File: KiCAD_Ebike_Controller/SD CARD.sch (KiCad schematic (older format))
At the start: 5 parts

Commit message: schem done
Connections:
- net labels removed: +3.3V
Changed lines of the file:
@@
 	3050 3300 3150 3400
-$Comp
-L power:+3.3V #PWR?
-U 1 1 5FAF998F
-P 5250 2750
-F 0 "#PWR?" H 5250 2600 50  0001 C CNN
-F 1 "+3.3V" H 5265 2923 50  0000 C CNN
-F 2 "" H 5250 2750 50  0001 C CNN
-F 3 "" H 5250 2750 50  0001 C CNN
-	1    5250 2750
-	1    0    0    -1
-$EndComp
 $Comp
 L power:GND #PWR?
@@
 Wire Wire Line
 	5400 3400 5100 3400
+Text Label 2950 1350 0    50   ~ 0
++3.3v
 Wire Bus Line
 	3050 3100 3050 3700
-Text Label 2950 1350 0    50   ~ 0
+Text Label 5250 2750 0    50   ~ 0
 +3.3v
 $EndSCHEMATC

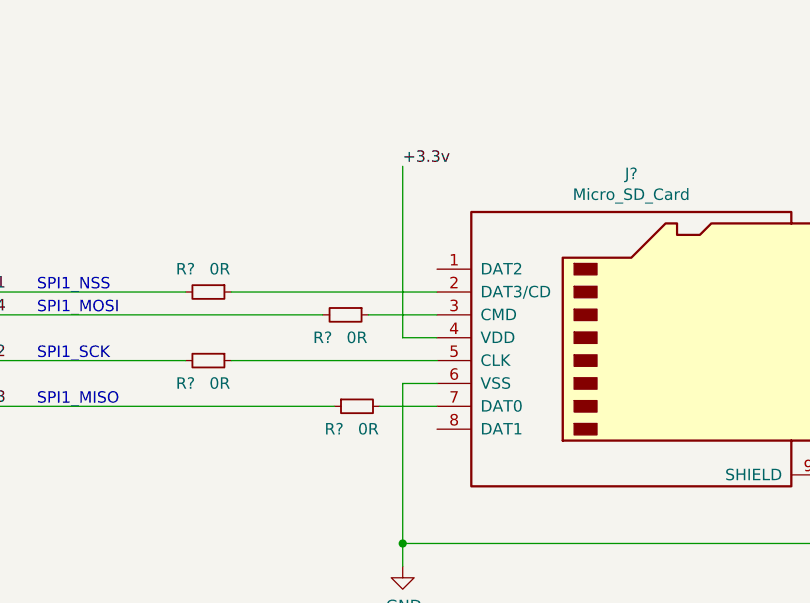
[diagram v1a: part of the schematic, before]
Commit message: adding footprints
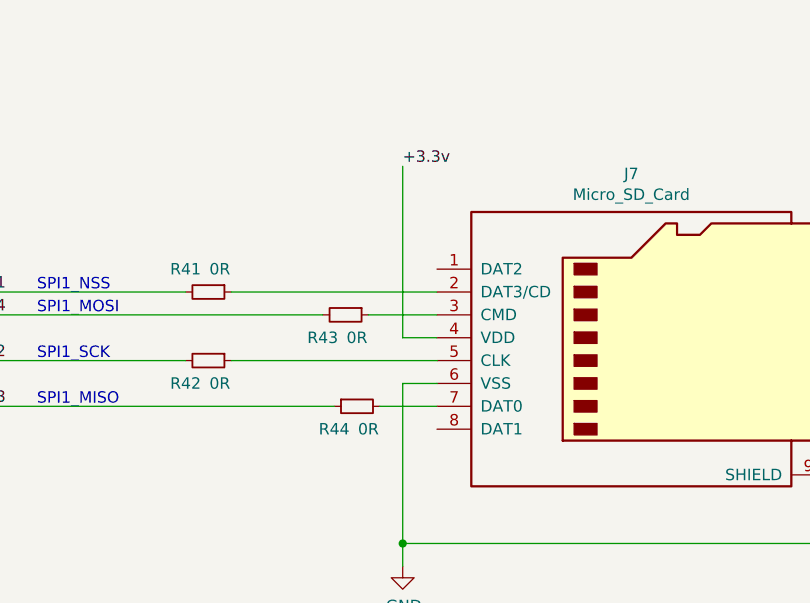
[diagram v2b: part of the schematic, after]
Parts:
- gave numbers to parts that had none: 5
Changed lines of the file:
@@
 	2950 1900 2950 2100
 $Comp
-L power:GND #PWR?
+L power:GND #PWR0129
 U 1 1 5FAEA30A
 P 2950 2100
-F 0 "#PWR?" H 2950 1850 50  0001 C CNN
+F 0 "#PWR0129" H 2950 1850 50  0001 C CNN
 F 1 "GND" H 2955 1927 50  0000 C CNN
 F 2 "" H 2950 2100 50  0001 C CNN
@@
 	3050 3300 3150 3400
 $Comp
-L power:GND #PWR?
+L power:GND #PWR0130
 U 1 1 5FAF9C96
 P 5250 4500
-F 0 "#PWR?" H 5250 4250 50  0001 C CNN
+F 0 "#PWR0130" H 5250 4250 50  0001 C CNN
 F 1 "GND" H 5255 4327 50  0000 C CNN
 F 2 "" H 5250 4500 50  0001 C CNN
@@
 	5250 4400 5250 4500
 $Comp
-L Connector:Micro_SD_Card J?
+L Connector:Micro_SD_Card J7
 U 1 1 5FAFB70A
 P 6300 3500
-F 0 "J?" H 6250 4217 50  0000 C CNN
+F 0 "J7" H 6250 4217 50  0000 C CNN
 F 1 "Micro_SD_Card" H 6250 4126 50  0000 C CNN
 F 2 "" H 7450 3800 50  0001 C CNN
@@
 $EndComp
 $Comp
-L Device:R_Small R?
+L Device:R_Small R41
 U 1 1 5FB009D5
 P 4400 3300
-F 0 "R?" V 4300 3200 50  0000 C CNN
+F 0 "R41" V 4300 3200 50  0000 C CNN
 F 1 "0R" V 4300 3350 50  0000 C CNN
 F 2 "" H 4400 3300 50  0001 C CNN
@@
 $EndComp
 $Comp
-L Device:R_Small R?
+L Device:R_Small R43
 U 1 1 5FB01074
 P 5000 3400
-F 0 "R?" V 5100 3300 50  0000 C CNN
+F 0 "R43" V 5100 3300 50  0000 C CNN
 F 1 "0R" V 5100 3450 50  0000 C CNN
 F 2 "" H 5000 3400 50  0001 C CNN
@@
 $EndComp
 $Comp
-L Device:R_Small R?
+L Device:R_Small R42
 U 1 1 5FB01354
 P 4400 3600
-F 0 "R?" V 4500 3500 50  0000 C CNN
+F 0 "R42" V 4500 3500 50  0000 C CNN
 F 1 "0R" V 4500 3650 50  0000 C CNN
 F 2 "" H 4400 3600 50  0001 C CNN
@@
 $EndComp
 $Comp
-L Device:R_Small R?
+L Device:R_Small R44
 U 1 1 5FB0153E
 P 5050 3800
-F 0 "R?" V 5150 3900 50  0000 C CNN
+F 0 "R44" V 5150 3900 50  0000 C CNN
 F 1 "0R" V 5150 3750 50  0000 C CNN
 F 2 "" H 5050 3800 50  0001 C CNN

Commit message: 50% of the way through the layout
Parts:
- J7: footprint (none) -> Connector_Card:microSD_HC_Hirose_DM3D-SF
- R41, R42, R43, R44: footprint (none) -> Resistor_SMD:R_0805_2012Metric_Pad1.15x1.40mm_HandSolder
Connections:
- net 3.3V+ renamed +3.3V
- net GND renamed GNDD
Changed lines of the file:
@@
 $Descr A4 11693 8268
 encoding utf-8
-Sheet 5 7
+Sheet 6 7
 Title ""
 Date ""
@@
 SPI
 Text HLabel 2500 1500 0    50   Input ~ 0
-3.3V+
++3.3V
 Wire Wire Line
 	2950 1500 2950 1350
@@
 Wire Wire Line
 	2950 1900 2950 2100
-$Comp
-L power:GND #PWR0129
-U 1 1 5FAEA30A
-P 2950 2100
-F 0 "#PWR0129" H 2950 1850 50  0001 C CNN
-F 1 "GND" H 2955 1927 50  0000 C CNN
-F 2 "" H 2950 2100 50  0001 C CNN
-F 3 "" H 2950 2100 50  0001 C CNN
-	1    2950 2100
-	1    0    0    -1
-$EndComp
 Wire Bus Line
 	2400 3100 3050 3100
@@
 Entry Wire Line
 	3050 3300 3150 3400
-$Comp
-L power:GND #PWR0130
-U 1 1 5FAF9C96
-P 5250 4500
-F 0 "#PWR0130" H 5250 4250 50  0001 C CNN
-F 1 "GND" H 5255 4327 50  0000 C CNN
-F 2 "" H 5250 4500 50  0001 C CNN
-F 3 "" H 5250 4500 50  0001 C CNN
-	1    5250 4500
-	1    0    0    -1
-$EndComp
 Wire Wire Line
 	7100 4100 7200 4100
@@
 F 0 "J7" H 6250 4217 50  0000 C CNN
 F 1 "Micro_SD_Card" H 6250 4126 50  0000 C CNN
-F 2 "" H 7450 3800 50  0001 C CNN
+F 2 "Connector_Card:microSD_HC_Hirose_DM3D-SF" H 7450 3800 50  0001 C CNN
 F 3 "http://katalog.we-online.de/em/datasheet/693072010801.pdf" H 6300 3500 50  0001 C CNN
 	1    6300 3500
@@
 F 0 "R41" V 4300 3200 50  0000 C CNN
 F 1 "0R" V 4300 3350 50  0000 C CNN
-F 2 "" H 4400 3300 50  0001 C CNN
+F 2 "Resistor_SMD:R_0805_2012Metric_Pad1.15x1.40mm_HandSolder" H 4400 3300 50  0001 C CNN
 F 3 "~" H 4400 3300 50  0001 C CNN
 	1    4400 3300
@@
 F 0 "R43" V 5100 3300 50  0000 C CNN
 F 1 "0R" V 5100 3450 50  0000 C CNN
-F 2 "" H 5000 3400 50  0001 C CNN
+F 2 "Resistor_SMD:R_0805_2012Metric_Pad1.15x1.40mm_HandSolder" H 5000 3400 50  0001 C CNN
 F 3 "~" H 5000 3400 50  0001 C CNN
 	1    5000 3400
@@
 F 0 "R42" V 4500 3500 50  0000 C CNN
 F 1 "0R" V 4500 3650 50  0000 C CNN
-F 2 "" H 4400 3600 50  0001 C CNN
+F 2 "Resistor_SMD:R_0805_2012Metric_Pad1.15x1.40mm_HandSolder" H 4400 3600 50  0001 C CNN
 F 3 "~" H 4400 3600 50  0001 C CNN
 	1    4400 3600
@@
 F 0 "R44" V 5150 3900 50  0000 C CNN
 F 1 "0R" V 5150 3750 50  0000 C CNN
-F 2 "" H 5050 3800 50  0001 C CNN
+F 2 "Resistor_SMD:R_0805_2012Metric_Pad1.15x1.40mm_HandSolder" H 5050 3800 50  0001 C CNN
 F 3 "~" H 5050 3800 50  0001 C CNN
 	1    5050 3800
@@
 Text Label 2950 1350 0    50   ~ 0
 +3.3v
+Text Label 5250 2750 0    50   ~ 0
++3.3v
 Wire Bus Line
 	3050 3100 3050 3700
-Text Label 5250 2750 0    50   ~ 0
-+3.3v
+$Comp
+L power:GNDD #PWR0130
+U 1 1 5FEADF63
+P 2950 2100
+F 0 "#PWR0130" H 2950 1850 50  0001 C CNN
+F 1 "GNDD" H 2954 1945 50  0000 C CNN
+F 2 "" H 2950 2100 50  0001 C CNN
+F 3 "" H 2950 2100 50  0001 C CNN
+	1    2950 2100
+	1    0    0    -1
+$EndComp
+Text HLabel 5250 4500 0    50   Input ~ 0
+GND
 $EndSCHEMATC

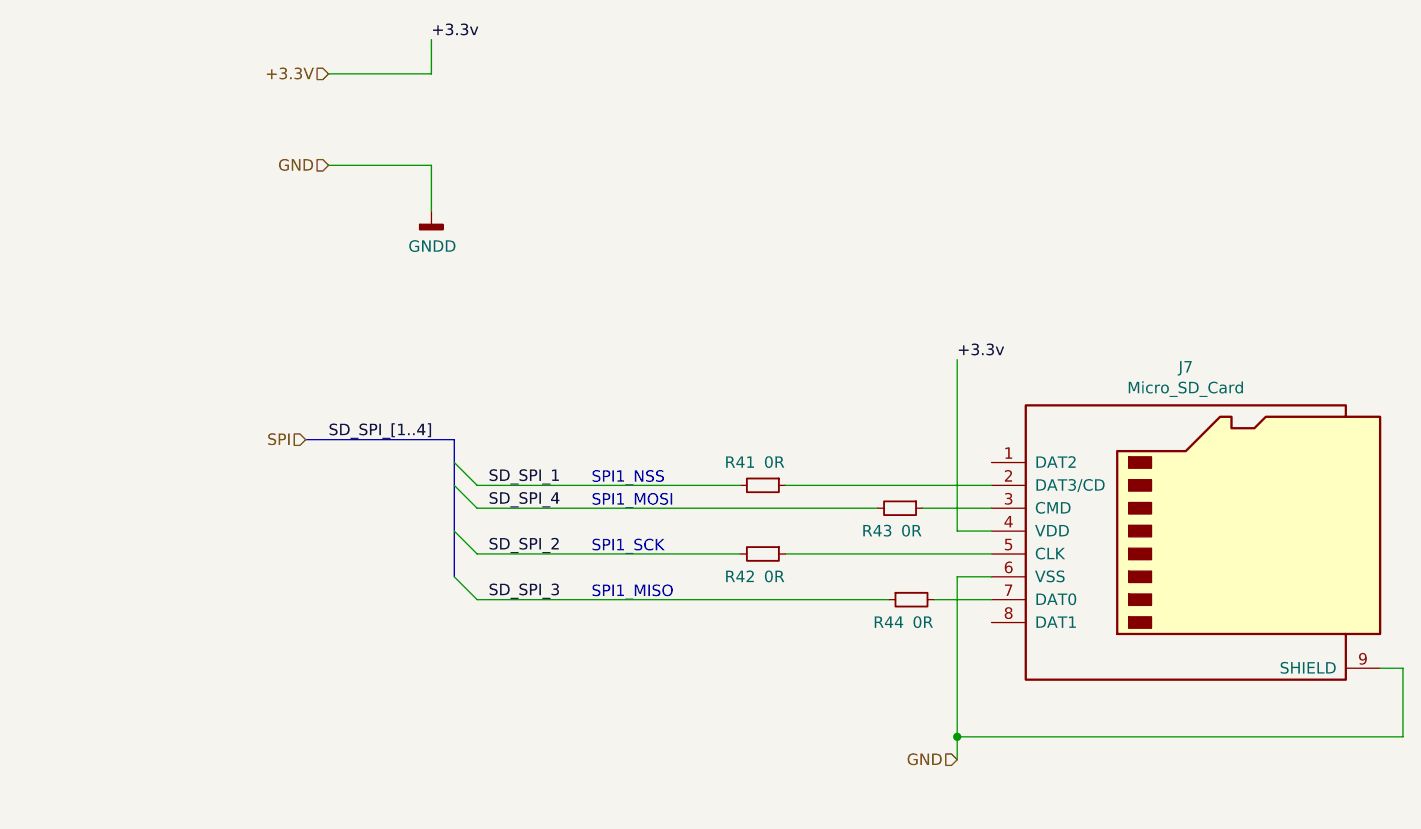
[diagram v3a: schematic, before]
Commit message: Layout done. will tidy up ref des next
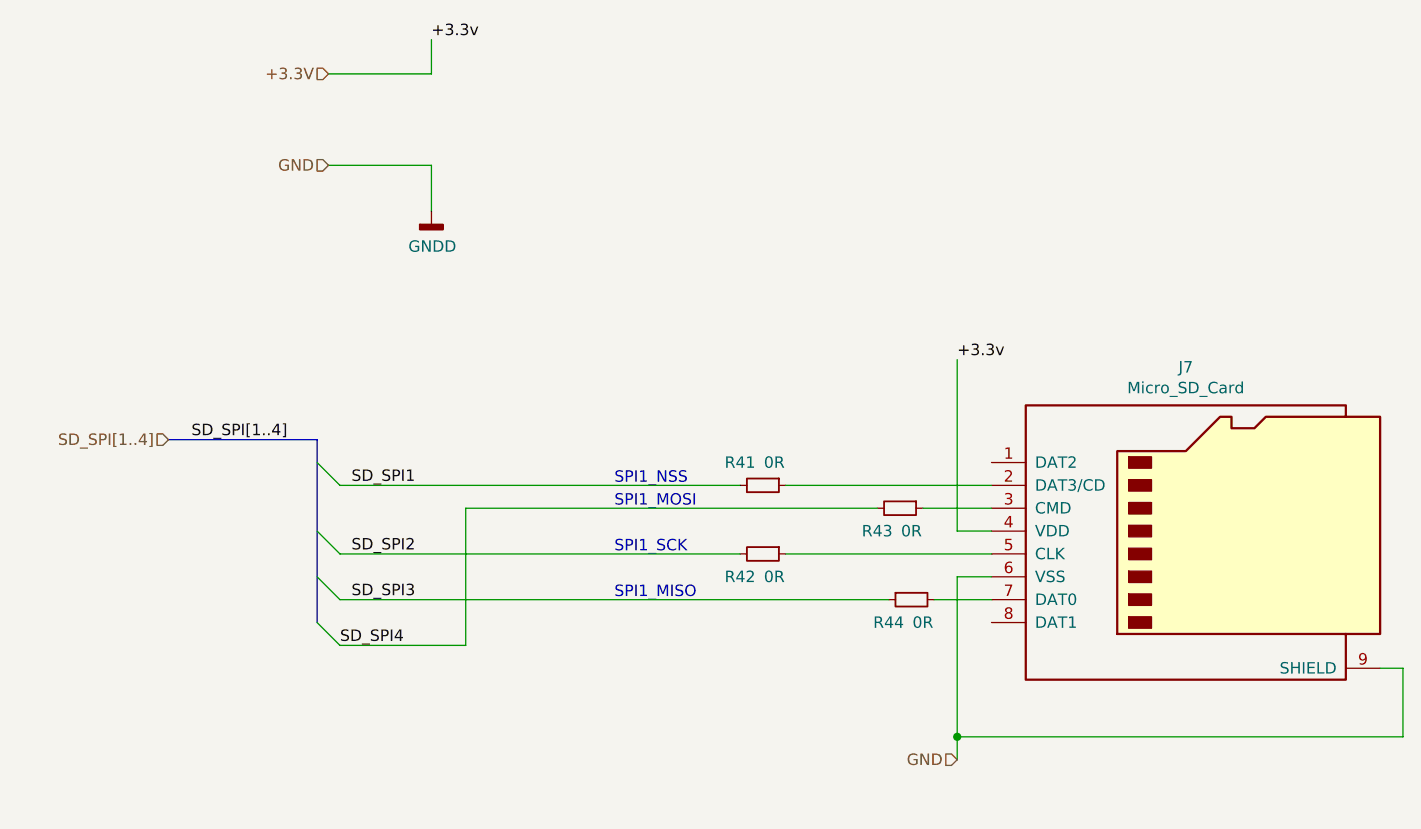
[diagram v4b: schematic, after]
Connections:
- net SD_SPI_1 renamed SD_SPI1
- net SD_SPI_2 renamed SD_SPI2
- net SD_SPI_3 renamed SD_SPI3
- net SD_SPI_4 renamed SD_SPI4
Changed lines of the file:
@@
 $Descr A4 11693 8268
 encoding utf-8
-Sheet 6 7
+Sheet 5 7
 Title ""
 Date ""
@@
 Text HLabel 2500 1900 0    50   Input ~ 0
 GND
-Text HLabel 2400 3100 0    50   Input ~ 0
-SPI
+Text HLabel 1800 3100 0    50   Input ~ 0
+SD_SPI[1..4]
 Text HLabel 2500 1500 0    50   Input ~ 0
 +3.3V
@@
 	2950 1900 2950 2100
 Wire Bus Line
-	2400 3100 3050 3100
+	1800 3100 2450 3100
 Entry Wire Line
-	3050 3200 3150 3300
+	2450 3200 2550 3300
 Entry Wire Line
-	3050 3500 3150 3600
+	2450 3500 2550 3600
 Entry Wire Line
-	3050 3700 3150 3800
-Text Label 2500 3100 0    50   ~ 0
-SD_SPI_[1..4]
-Text Label 3200 3300 0    50   ~ 0
-SD_SPI_1
-Text Notes 3650 3300 0    50   ~ 0
+	2450 3700 2550 3800
+Text Label 1900 3100 0    50   ~ 0
+SD_SPI[1..4]
+Text Label 2600 3300 0    50   ~ 0
+SD_SPI1
+Text Notes 3750 3300 0    50   ~ 0
 SPI1_NSS
-Text Label 3200 3600 0    50   ~ 0
-SD_SPI_2
-Text Label 3200 3800 0    50   ~ 0
-SD_SPI_3
-Text Label 3200 3400 0    50   ~ 0
-SD_SPI_4
+Text Label 2600 3600 0    50   ~ 0
+SD_SPI2
+Text Label 2600 3800 0    50   ~ 0
+SD_SPI3
+Text Label 2550 4000 0    50   ~ 0
+SD_SPI4
 Wire Wire Line
 	5400 3500 5250 3500
@@
 Wire Wire Line
 	5250 3700 5250 4400
-Text Notes 3650 3600 0    50   ~ 0
+Text Notes 3750 3600 0    50   ~ 0
 SPI1_SCK
-Text Notes 3650 3800 0    50   ~ 0
+Text Notes 3750 3800 0    50   ~ 0
 SPI1_MISO
-Text Notes 3650 3400 0    50   ~ 0
+Text Notes 3750 3400 0    50   ~ 0
 SPI1_MOSI
 Entry Wire Line
-	3050 3300 3150 3400
+	2450 3900 2550 4000
 Wire Wire Line
 	7100 4100 7200 4100
@@
 $EndComp
 Wire Wire Line
-	3150 3600 4300 3600
-Wire Wire Line
 	4500 3600 5400 3600
 Wire Wire Line
 	5400 3800 5150 3800
 Wire Wire Line
-	3150 3800 4950 3800
-Wire Wire Line
-	3150 3400 4900 3400
-Wire Wire Line
-	3150 3300 4300 3300
+	2550 3300 4300 3300
 Wire Wire Line
 	4500 3300 5400 3300
@@
 Text Label 5250 2750 0    50   ~ 0
 +3.3v
-Wire Bus Line
-	3050 3100 3050 3700
 $Comp
 L power:GNDD #PWR0130
@@
 Text HLabel 5250 4500 0    50   Input ~ 0
 GND
+Wire Wire Line
+	2550 4000 3100 4000
+Wire Wire Line
+	3100 4000 3100 3400
+Wire Wire Line
+	3100 3400 4900 3400
+Wire Wire Line
+	2550 3800 4950 3800
+Wire Wire Line
+	2550 3600 4300 3600
+Wire Bus Line
+	2450 3100 2450 3900
 $EndSCHEMATC
